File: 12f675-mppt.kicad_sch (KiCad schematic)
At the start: 45 parts, among them IC1 PIC12F629-I/P, J1 S+, J2 S-, J3 O+, J4 O-, Q1 BUK9511-55A127, Q2 BUK9511-55A127, Q3 2N2222A, Q4 2N2222A, Q5 2N2907A, SW1 Write OP-AMP DIFF, U1 LM7805_TO220, U2 LM358N

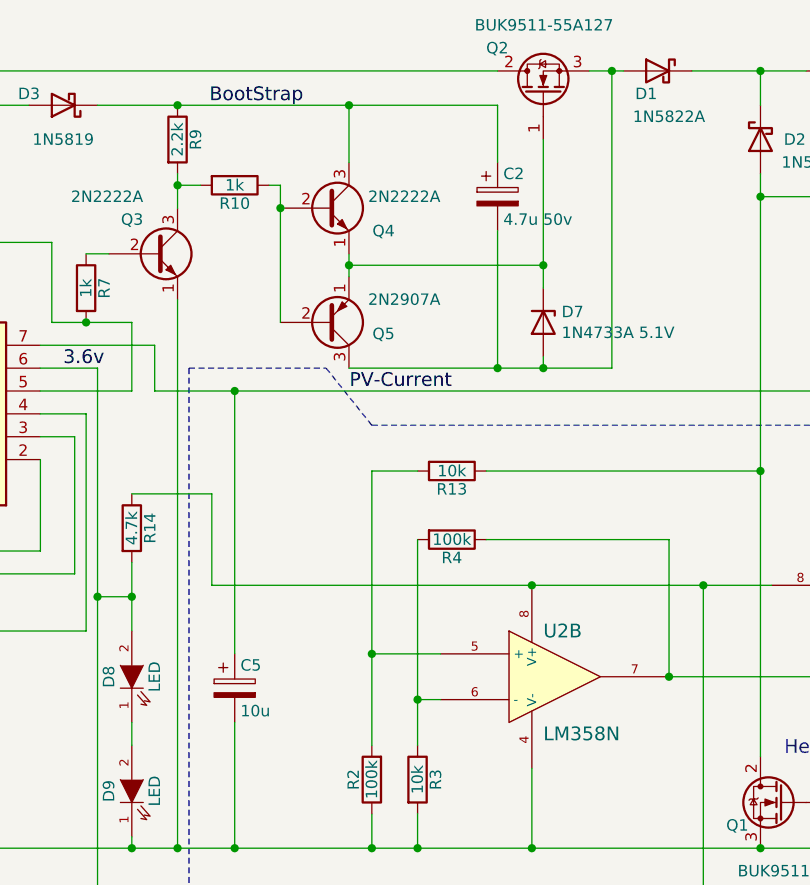
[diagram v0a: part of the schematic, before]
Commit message: Change capacitors.
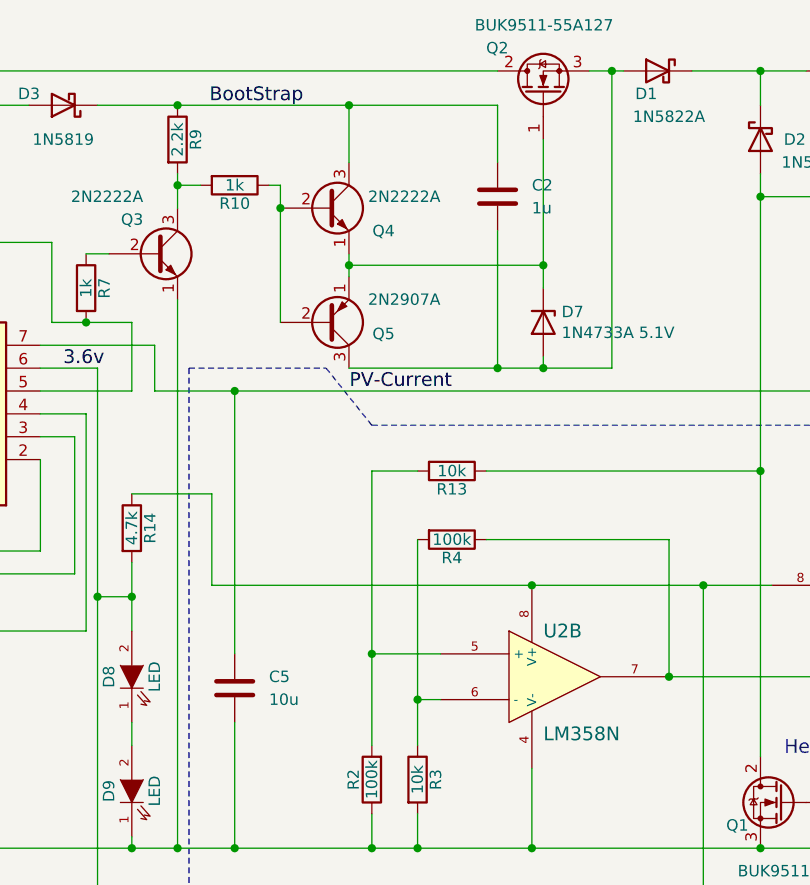
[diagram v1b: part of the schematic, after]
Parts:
- removed C2: 4.7u 50v, Capacitors_THT:CP_Radial_D12.5mm_P5.00mm, symbol Device:CP
- removed C5: 10u, Capacitors_THT:CP_Radial_D12.5mm_P5.00mm, symbol Device:CP
- added C2: 1u, Capacitors_THT:C_Disc_D7.5mm_W4.4mm_P5.00mm, symbol Device:C
- added C5: 10u, Capacitors_THT:C_Disc_D7.5mm_W4.4mm_P5.00mm, symbol Device:C
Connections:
- net BootStrap: now also C2.1
- net GNDPWR: now also C5.2
- net PV-Current: now also C5.1
- net at D1.2 (A), D7.2 (A), Q2.3 (S)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: now also C2.2
